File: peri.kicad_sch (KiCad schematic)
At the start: 23 parts, among them J10 Conn_02x08_Odd_Even, J11 Conn_01x08, J5 PeriHDR, J6 PI Mating connector, J8 I2C_EXT, Q1 2N7002, SW4 RP8100B2M1CEBLKBLKWHT

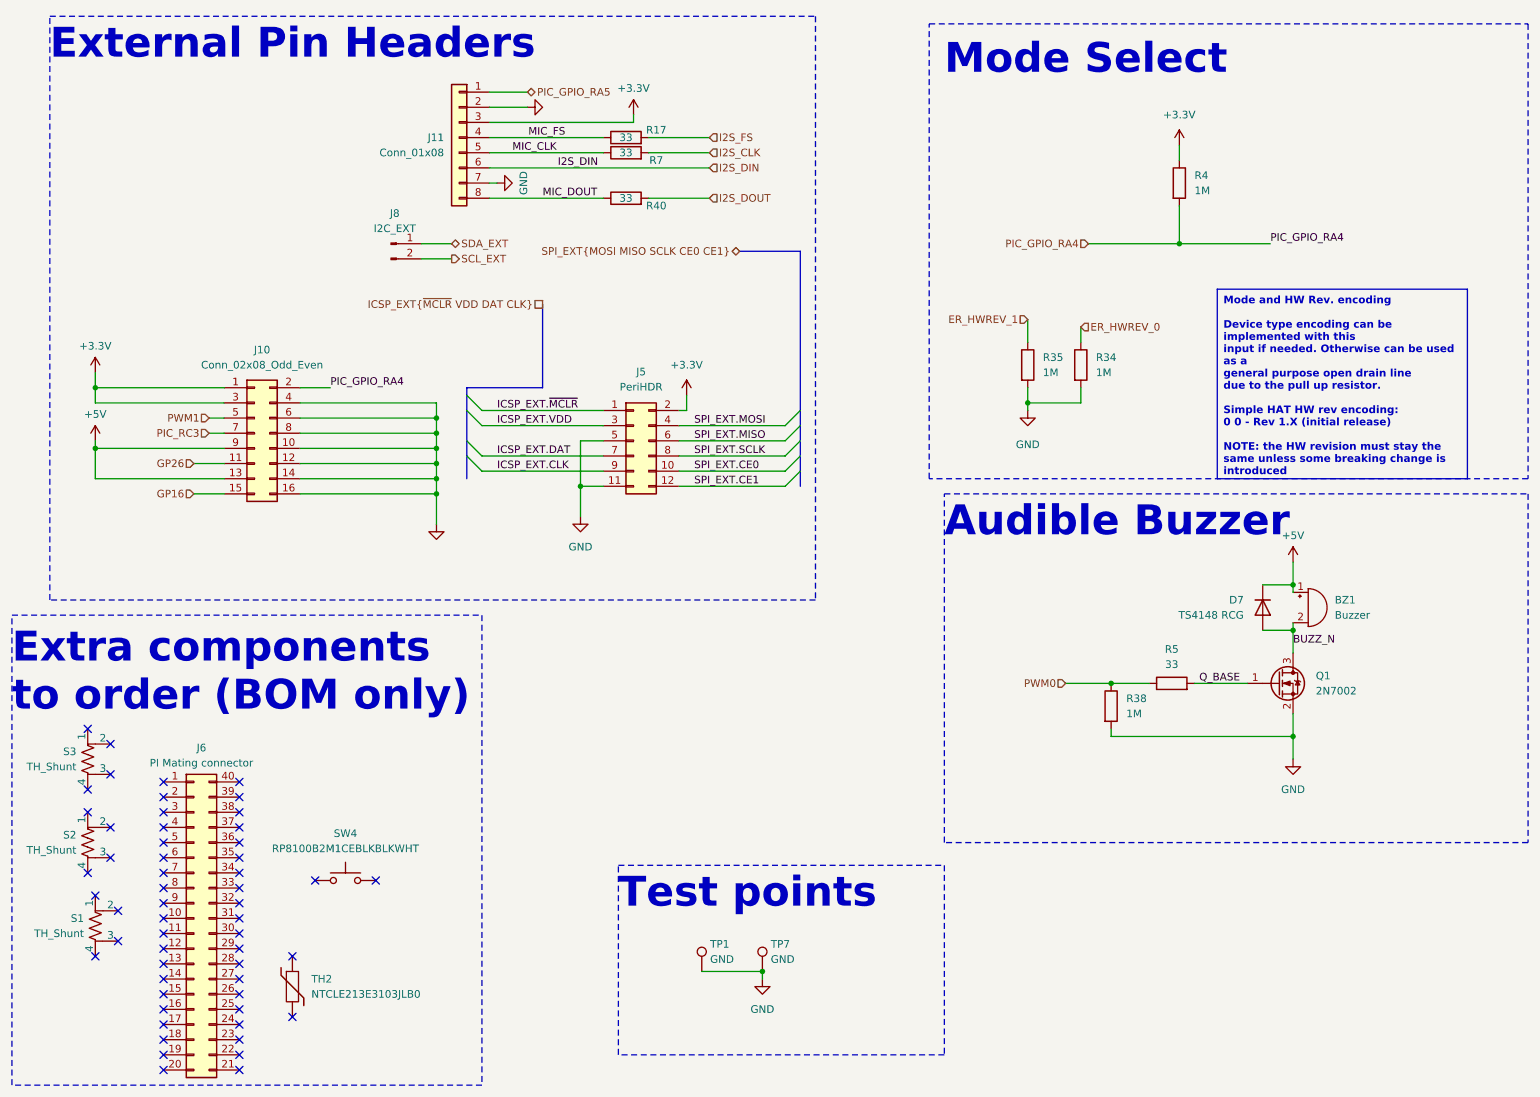
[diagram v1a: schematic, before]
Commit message: fix: modifications after driver completion
- Added missing RTC IRQ to PI
- RTC VBAT is not connected to the Main Battery trough a ~1k resistor
- Connected BQ CE through a Push-pull to Open-Drain converter to PI
- Changed Mosfets to TI PicoStar model
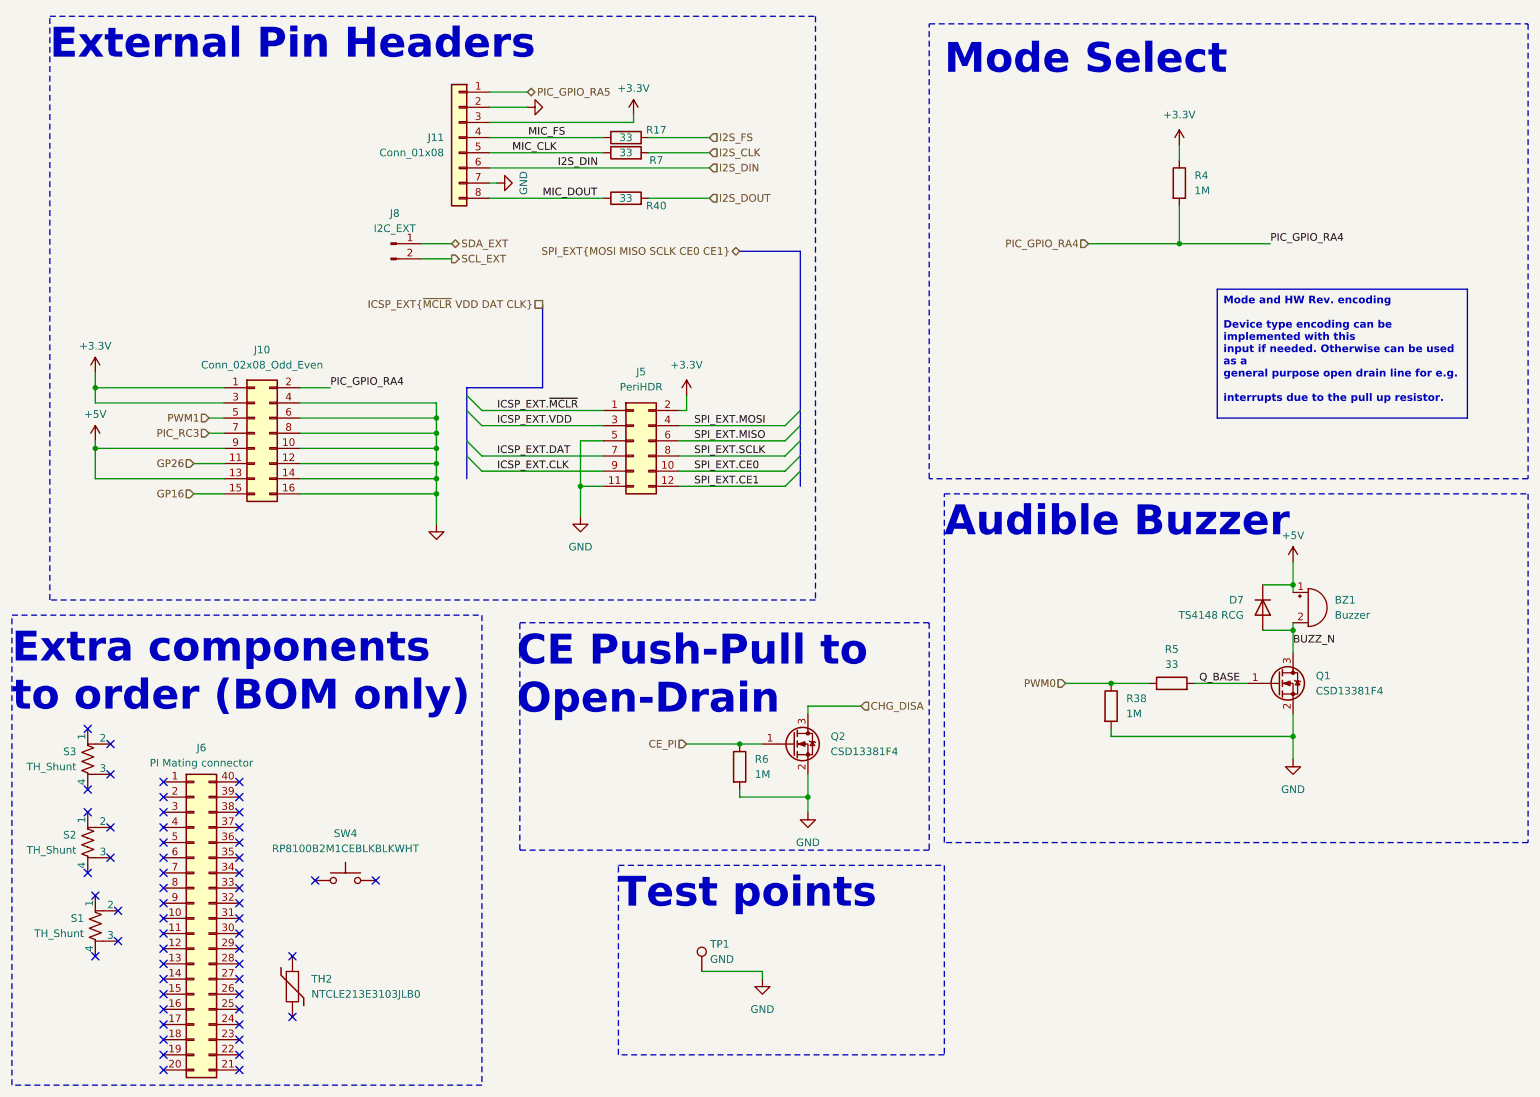
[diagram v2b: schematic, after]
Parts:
- removed R34, R35: 1M, Resistor_SMD:R_0402_1005Metric, symbol Device:R
- removed TP7: GND, TestPoint:TestPoint_Pad_D1.0mm, symbol Connector:TestPoint
- added Q2: CSD13381F4, effectiveRangeHat:YJC0003A_TEX, symbol Transistor_FET:2N7002
- added R6: 1M, Resistor_SMD:R_0402_1005Metric, symbol Device:R
- Q1: value 2N7002 -> CSD13381F4; footprint Package_TO_SOT_SMD:SOT-23 -> effectiveRangeHat:YJC0003A_TEX; MPN 2N7002 -> CSD13381F4; Manufacturer onsemi -> Texas Instruments
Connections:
- net GND: now also Q2.2 (S), R6.2
- new net CE_PI: Q2.1 (G), R6.1
- new net CHG_DISA: Q2.3 (D)
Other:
- note added: "CE Push-Pull to Open-Drain"

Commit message: fix: pcb changes, moved i2c ext header to 2x2 pin at the edge, pinout adjustments, silkscreen fixes
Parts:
- removed J8: I2C_EXT, Connector_PinHeader_2.54mm:PinHeader_1x02_P2.54mm_Vertical, symbol Connector:Conn_01x02_Pin
- added J7: PWR_HDR, Connector_PinHeader_2.54mm:PinHeader_2x02_P2.54mm_Vertical, symbol Connector_Generic:Conn_02x02_Odd_Even
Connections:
- net PIC_RC3: now also J10.5 (Pin_5); no longer J10.7 (Pin_7)
- net PWM1: now also J10.7 (Pin_7); no longer J10.5 (Pin_5)
- net SCL_EXT: now also J7.4 (Pin_4)
- net SDA_EXT: now also J7.2 (Pin_2)
- new net NCT_TH_1: J7.1 (Pin_1)
- new net NCT_TH_2: J7.3 (Pin_3)
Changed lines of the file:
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@@
 		)
 	)
-	(wire
-		(pts
-			(xy 88.9 55.88) (xy 83.82 55.88)
-		)
-		(stroke
-			(width 0)
-			(type default)
-		)
-	)
 	(bus
 		(pts
@@
 	(wire
 		(pts
+			(xy 68.58 55.88) (xy 71.12 55.88)
+		)
+		(stroke
+			(width 0)
+			(type default)
+		)
+	)
+	(wire
+		(pts
 			(xy 224.79 113.03) (xy 229.87 113.03)
 		)
@@
 	(wire
 		(pts
-			(xy 88.9 58.42) (xy 83.82 58.42)
+			(xy 71.12 58.42) (xy 68.58 58.42)
+		)
+		(stroke
+			(width 0)
+			(type default)
+		)
+	)
+	(wire
+		(pts
+			(xy 54.61 58.42) (xy 55.88 58.42)
 		)
 		(stroke
@@
 	(wire
 		(pts
+			(xy 54.61 55.88) (xy 55.88 55.88)
+		)
+		(stroke
+			(width 0)
+			(type default)
+		)
+	)
+	(wire
+		(pts
 			(xy 127 93.98) (xy 144.78 93.98)
 		)
@@
 		)
 	)
+	(hierarchical_label "NCT_TH_1"
+		(shape passive)
+		(at 54.61 55.88 180)
+		(fields_autoplaced yes)
+		(effects
+			(font
+				(size 1.27 1.27)
+			)
+			(justify right)
+		)
+	)
 	(hierarchical_label "PIC_RC3"
 		(shape input)
-		(at 48.26 87.63 180)
+		(at 48.26 85.09 180)
 		(fields_autoplaced yes)
 		(effects
@@
 	(hierarchical_label "SCL_EXT"
 		(shape output)
-		(at 88.9 58.42 0)
+		(at 71.12 58.42 0)
 		(fields_autoplaced yes)
 		(effects
@@
 	(hierarchical_label "SDA_EXT"
 		(shape bidirectional)
-		(at 88.9 55.88 0)
+		(at 71.12 55.88 0)
 		(fields_autoplaced yes)
 		(effects
@@
 		)
 	)
+	(hierarchical_label "NCT_TH_2"
+		(shape passive)
+		(at 54.61 58.42 180)
+		(fields_autoplaced yes)
+		(effects
+			(font
+				(size 1.27 1.27)
+			)
+			(justify right)
+		)
+	)
 	(hierarchical_label "I2S_DIN"
 		(shape input)
@@
 	(hierarchical_label "PWM1"
 		(shape input)
-		(at 48.26 85.09 180)
+		(at 48.26 87.63 180)
 		(fields_autoplaced yes)
 		(effects
@@
 	)
 	(symbol
-		(lib_id "Connector:Conn_01x02_Pin")
-		(at 78.74 55.88 0)
-		(unit 1)
-		(exclude_from_sim no)
-		(in_bom yes)
-		(on_board yes)
-		(dnp no)
-		(fields_autoplaced yes)
-		(property "Reference" "J8"
-			(at 79.375 50.8 0)
-			(effects
-				(font
-					(size 1.27 1.27)
-				)
-			)
-		)
-		(property "Value" "I2C_EXT"
-			(at 79.375 53.34 0)
-			(effects
-				(font
-					(size 1.27 1.27)
-				)
-			)
-		)
-		(property "Footprint" "Connector_PinHeader_2.54mm:PinHeader_1x02_P2.54mm_Vertical"
-			(at 78.74 55.88 0)
-			(effects
-				(font
-					(size 1.27 1.27)
-				)
-				(hide yes)
-			)
-		)
-		(property "Datasheet" "~"
-			(at 78.74 55.88 0)
-			(effects
-				(font
-					(size 1.27 1.27)
-				)
-				(hide yes)
-			)
-		)
-		(property "Description" "Generic connector, single row, 01x02, script generated"
-			(at 78.74 55.88 0)
-			(effects
-				(font
-					(size 1.27 1.27)
-				)
-				(hide yes)
-			)
-		)
-		(property "MPN" "61300211121"
-			(at 78.74 55.88 0)
-			(effects
-				(font
-					(size 1.27 1.27)
-				)
-				(hide yes)
-			)
-		)
-		(property "Manufacturer" "Würth Elektronik"
-			(at 78.74 55.88 0)
-			(effects
-				(font
-					(size 1.27 1.27)
-				)
-				(hide yes)
-			)
-		)
-		(property "Manufaturer" ""
-			(at 78.74 55.88 0)
-			(effects
-				(font
-					(size 1.27 1.27)
-				)
-				(hide yes)
-			)
-		)
-		(pin "1"
-		)
-		(pin "2"
-		)
-		(instances
-			(project "effectiveRangeHat_simple"
-				(path "/6edc5e63-ec2a-49cc-8eeb-48e0d5e90dc6/53f70a5b-3679-49fb-a930-7f86bae1d9a8"
-					(reference "J8")
-					(unit 1)
-				)
-			)
-		)
-	)
-	(symbol
 		(lib_id "Switch:SW_Push")
 		(at 71.12 162.56 0)
@@
 					(unit 1)
 				)
+			)
+		)
+	)
+	(symbol
+		(lib_id "Connector_Generic:Conn_02x02_Odd_Even")
+		(at 60.96 55.88 0)
+		(unit 1)
+		(exclude_from_sim no)
+		(in_bom yes)
+		(on_board yes)
+		(dnp no)
+		(fields_autoplaced yes)
+		(property "Reference" "J7"
+			(at 62.23 49.403 0)
+			(effects
+				(font
+					(size 1.27 1.27)
+				)
+			)
+		)
+		(property "Value" "PWR_HDR"
+			(at 62.23 51.943 0)
+			(effects
+				(font
+					(size 1.27 1.27)
+				)
+			)
+		)
+		(property "Footprint" "Connector_PinHeader_2.54mm:PinHeader_2x02_P2.54mm_Vertical"
+			(at 60.96 55.88 0)
+			(effects
+				(font
+					(size 1.27 1.27)
+				)
+				(hide yes)
+			)
+		)
+		(property "Datasheet" "~"
+			(at 60.96 55.88 0)
+			(effects
+				(font
+					(size 1.27 1.27)
+				)
+				(hide yes)
+			)
+		)
+		(property "Description" "Generic connector, double row, 02x02, odd/even pin numbering scheme (row 1 odd numbers, row 2 even numbers), script generated (kicad-library-utils/schlib/autogen/connector/)"
+			(at 60.96 55.88 0)
+			(effects
+				(font
+					(size 1.27 1.27)
+				)
+				(hide yes)
+			)
+		)
+		(property "MPN" "61300421121"
+			(at 60.96 55.88 0)
+			(effects
+				(font
+					(size 1.27 1.27)
+				)
+				(hide yes)
+			)
+		)
+		(property "Manufacturer" "Würth Elektronik"
+			(at 60.96 55.88 0)
+			(effects
+				(font
+					(size 1.27 1.27)
+				)
+				(hide yes)
+			)
+		)
+		(property "SupplierLink" "https://www.digikey.hu/en/products/detail/w%C3%BCrth-elektronik/61300421121/4846829"
+			(at 60.96 55.88 0)
+			(effects
+				(font
+					(size 1.27 1.27)
+				)
+				(hide yes)
+			)
+		)
+		(property "Note" "TH"
+			(at 60.96 55.88 0)
+			(effects
+				(font
+					(size 1.27 1.27)
+				)
+				(hide yes)
+			)
+		)
+		(property "Manufaturer" ""
+			(at 60.96 55.88 0)
+			(effects
+				(font
+					(size 1.27 1.27)
+				)
+				(hide yes)
+			)
+		)
+		(pin "1"
+		)
+		(pin "2"
+		)
+		(pin "3"
+		)
+		(pin "4"
+		)
+		(instances
+			(project "effectiveRangeHat_simple"
+				(path "/6edc5e63-ec2a-49cc-8eeb-48e0d5e90dc6/53f70a5b-3679-49fb-a930-7f86bae1d9a8"
+					(reference "J7")
+					(unit 1)
+				)
